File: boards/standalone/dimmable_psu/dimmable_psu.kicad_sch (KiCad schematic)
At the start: 87 parts, among them J1 DIM_IN, J2 PWM_IN, J3 POWER, J4 POWER_OUT, Q1 2N7002, Q2 BST52, Q3 BST52, Q4 IRF540N, Q5 IRF540N, SW1 SW_DIP_SPLIT_x02, U1 LM324, U2 LMC7660, U3 TPS92640

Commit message: rearrange
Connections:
- net OUT+: now also J4.1 (Pin_1); no longer J4.2 (Pin_2)
- net OUT-: now also J4.2 (Pin_2); no longer J4.1 (Pin_1)
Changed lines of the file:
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@@
-(kicad_sch (version 20210126) (generator eeschema)
+(kicad_sch (version 20210406) (generator eeschema)
   (paper "A3")
   (title_block
@@
     (pin "2")
   )
-  (symbol (lib_id "Connector_Generic:Conn_01x02") (at 379.73 80.01 0) (mirror x) (unit 1)
-    (in_bom yes) (on_board yes)
-    (property "Reference" "J4" (id 0) (at 382.27 80.01 0)
-      (effects (font (size 1.27 1.27)) (justify left))
-    )
-    (property "Value" "POWER_OUT" (id 1) (at 382.27 77.47 0)
-      (effects (font (size 1.27 1.27)) (justify left))
-    )
-    (property "Footprint" "wago:2061-602" (id 2) (at 379.73 80.01 0)
-      (effects (font (size 1.27 1.27)) hide)
-    )
-    (property "Datasheet" "~" (id 3) (at 379.73 80.01 0)
-      (effects (font (size 1.27 1.27)) hide)
-    )
+  (symbol (lib_id "Connector_Generic:Conn_01x02") (at 379.73 77.47 0) (unit 1)
+    (in_bom yes) (on_board yes)
+    (property "Reference" "J4" (id 0) (at 382.27 77.47 0)
+      (effects (font (size 1.27 1.27)) (justify left))
+    )
+    (property "Value" "POWER_OUT" (id 1) (at 382.27 80.01 0)
+      (effects (font (size 1.27 1.27)) (justify left))
+    )
+    (property "Footprint" "wago:2061-602" (id 2) (at 379.73 77.47 0)
+      (effects (font (size 1.27 1.27)) hide)
+    )
+    (property "Datasheet" "~" (id 3) (at 379.73 77.47 0)
+      (effects (font (size 1.27 1.27)) hide)
+    )

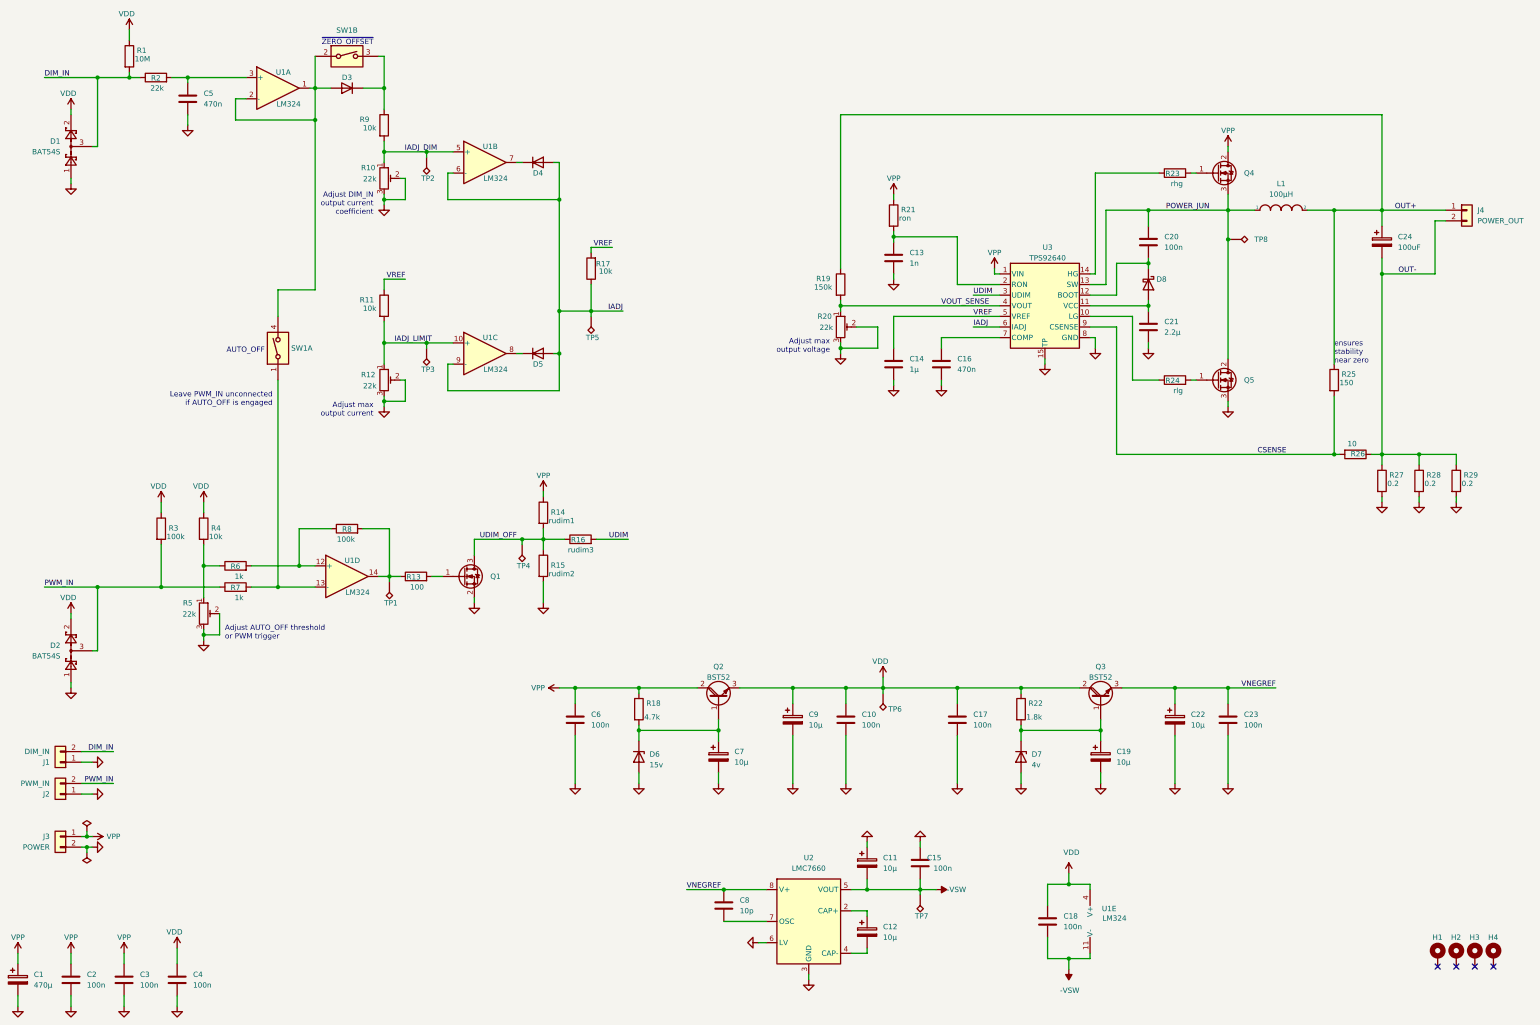
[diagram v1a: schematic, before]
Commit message: overvoltage limit resistor
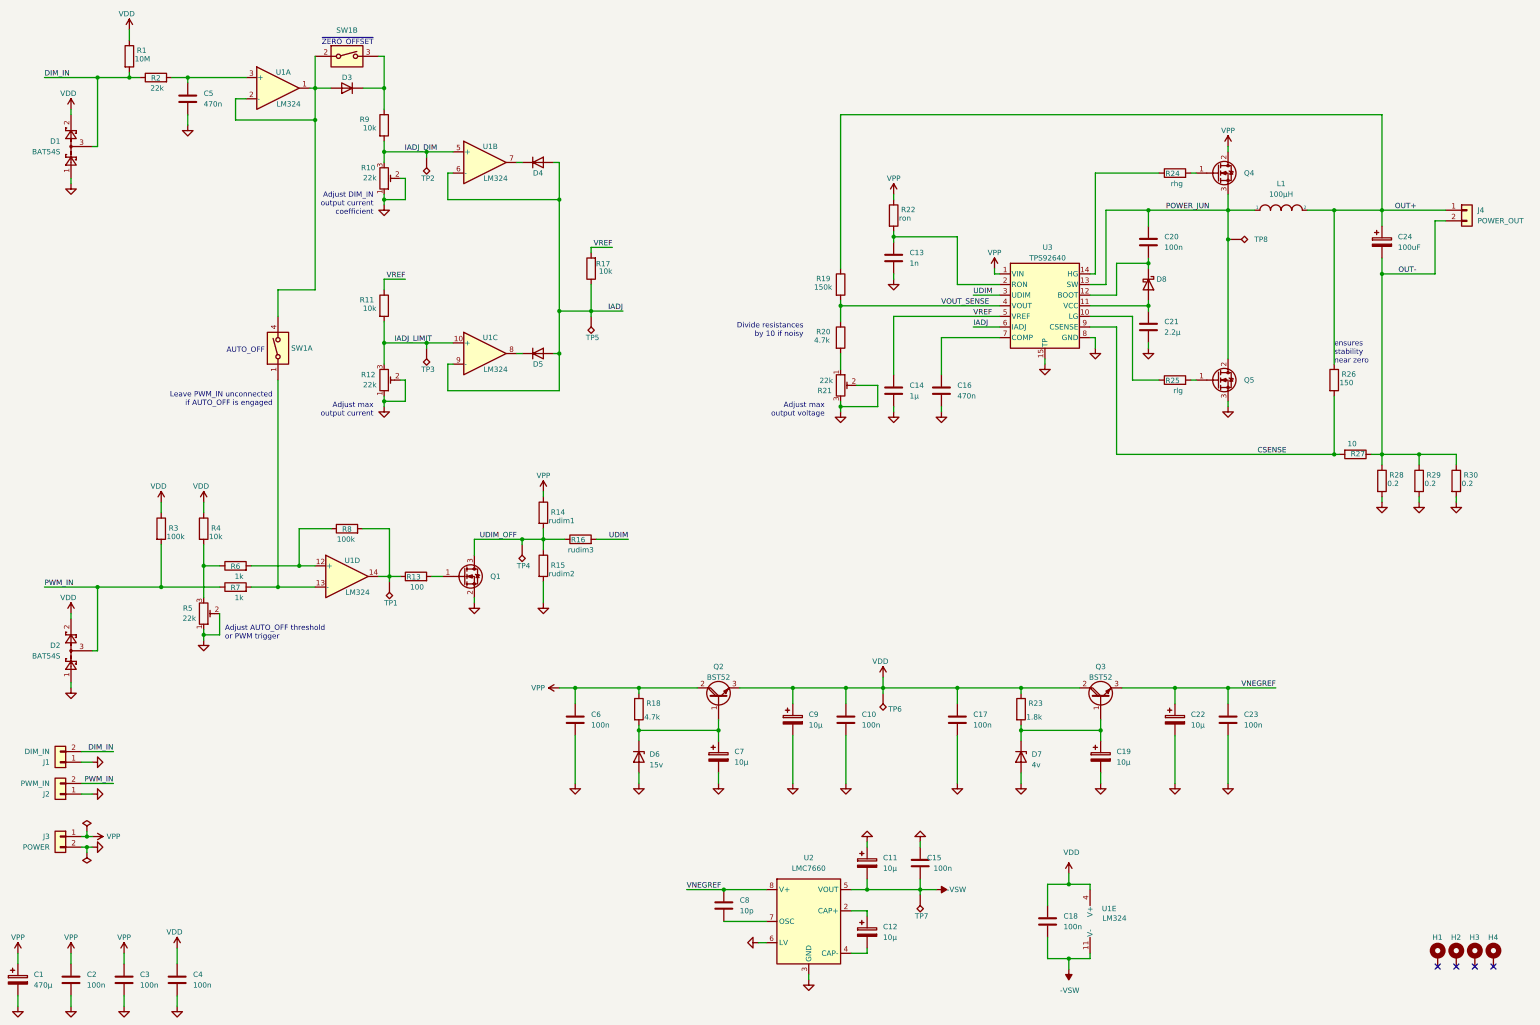
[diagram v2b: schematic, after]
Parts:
- added R20: 4.7k, Resistor_SMD:R_0805_2012Metric_Pad1.20x1.40mm_HandSolder, symbol Device:R
- renumbered R20 to R21, R21 to R22, R22 to R23, R23 to R24, R24 to R25, R25 to R26, R26 to R27, R27 to R28, R28 to R29, R29 to R30
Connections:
- net GND: now also R10.1, R12.1, R5.1; no longer R10.3, R12.3, R5.3
- net IADJ_DIM: now also R10.3; no longer R10.1
- net IADJ_LIMIT: now also R12.3; no longer R12.1
- net VOUT_SENSE: now also R20.1; no longer R21.1
- net at R4.2, R6.1: now also R5.3; no longer R5.1
- new net: R20.2, R21.1
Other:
- note added: "Divide resistances by 10 if noisy"
- moved on the sheet: C14, C16, R21
